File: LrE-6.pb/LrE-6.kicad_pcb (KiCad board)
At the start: 2 copper layers, 100 x 100 mm, 112 parts, among them J1 USB_B_Micro, J2 SM06B-SRSS-TB, Q1 2N7002, SW1 Tact_SW_8mm, SW10 Tact_SW_8mm, SW11 EC11_SMD, SW12 EC11_SMD, SW13 EC11_SMD, SW14 EC11_SMD, SW15 EC11_SMD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

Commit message: First commit for F3.2PB
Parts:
- C1, C10, C11, C12, C2, C3, C4, C5, C6, C7, C8, C9, R10, R11, R12, R13, R14, R15, R16, R5, R6, R7, R8, R9: moved to B.Cu
- SW11, SW12, SW13, SW14, SW15, SW16: footprint LrE-6:RotaryEncoder_EC11E-SMD2 -> Rotary_Encoder:RotaryEncoder_Alps_EC11E-Switch_Vertical_H20mm
- moved D16 0.86 mm to (105.2, 167.0)
- moved R13 0.11 mm to (184.7, 155.4)
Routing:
- net GND: track 126.7 -> 136.7 mm, vias 63 -> 65
- net +3V3: track 414.9 -> 407.7 mm
- net /ENC4-A: track 95.6 -> 92.1 mm
- net /ENC5-B: track 112.5 -> 109.2 mm
- net Net-(D11-Pad2): track 3.71 -> 6.80 mm
- net /ENC1-B: track 84.1 -> 87.1 mm, vias 1 -> 0
- net /L0: track 121.9 -> 119.1 mm
- net /LED1OUT: track 35.4 -> 38.1 mm
- net /L3: track 132.9 -> 130.3 mm, vias 7 -> 4
- net /ENC2-B: track 54.0 -> 56.2 mm
- net /ENC2-A: track 43.5 -> 45.8 mm
- net /L2: track 158.4 -> 156.3 mm, vias 3 -> 2
- net Net-(D15-Pad2): track 2.90 -> 5.02 mm
- net /VBUS: track 265.8 -> 267.8 mm
- net Net-(D16-Pad2): track 2.31 -> 4.23 mm
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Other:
- board text added: "F3.2"
- board text removed: "-1"
- board text removed: "F2.8"

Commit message: F3.2 add coper por inhibit
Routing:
- net GND: vias 65 -> 66

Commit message: F3.2 commit for order pb
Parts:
- gave numbers to parts that had none: 1
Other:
- board text added: "OLED"
- board text added: "for MIDI2LR"

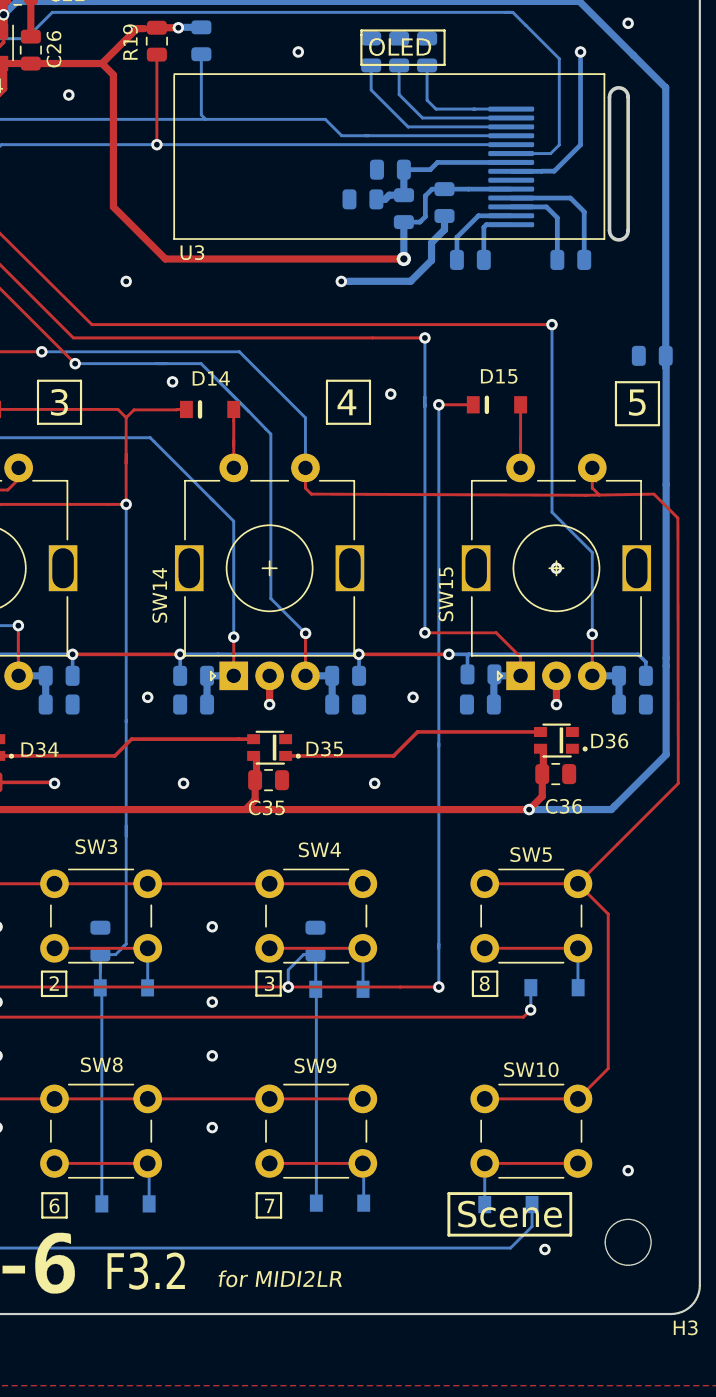
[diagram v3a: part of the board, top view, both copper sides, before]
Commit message: Rename LrE-6.pb F3.2 to F2.8-2
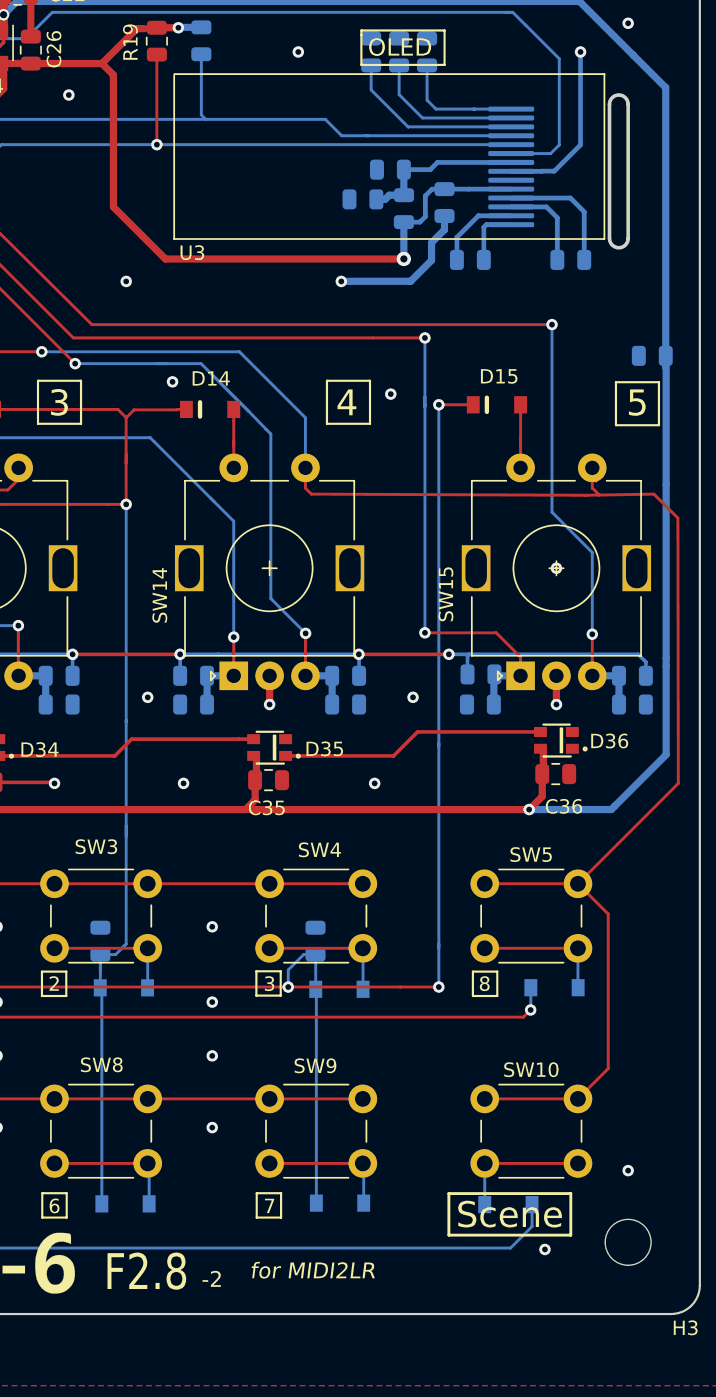
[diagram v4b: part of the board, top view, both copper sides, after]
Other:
- outline, holes or cut-outs redrawn
- board text added: "-2"
- board text added: "F2.8"
- board text removed: "F3.2"
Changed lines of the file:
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@@
-(kicad_pcb (version 20171130) (host pcbnew "(5.1.6)-1")
+(kicad_pcb (version 20171130) (host pcbnew "(5.1.6-0)")
   (general
     (thickness 1.2)
-    (drawings 120)
+    (drawings 121)
     (tracks 1270)
     (zones 0)
@@
     (add_net +3V3)
   )
+  (module LrE-6:OLED-9.1 locked (layer F.Cu)
+    (at 163.3462 113.5419)
+    (fp_text reference U3 (at 1.2638 12.4881) (layer F.SilkS)
+      (effects (font (size 1 1) (thickness 0.15)))
+    )
+    (fp_text value SSD1306_OLED_0.91 (at 8.9 -1.1) (layer F.Fab)
+      (effects (font (size 1 1) (thickness 0.15)))
+    )
+    (fp_circle (center 21 10.5) (end 21.2 10.5) (layer B.SilkS) (width 0.25))
+    (fp_line (start 30 0) (end 0 0) (layer F.SilkS) (width 0.12))
+    (fp_line (start 30 11.5) (end 30 0) (layer F.SilkS) (width 0.12))
+    (fp_line (start 0 11.5) (end 30 11.5) (layer F.SilkS) (width 0.12))
+    (fp_line (start 0 0.1) (end 0 11.5) (layer F.SilkS) (width 0.12))
+    (pad 11 smd roundrect (at 23.5 4.3) (size 3.2 0.35) (layers B.Cu B.Paste B.Mask) (roundrect_rratio 0.25)
+      (net 25 /SDA))
+    (pad 1 smd roundrect (at 23.5 10.5) (size 3.2 0.35) (layers B.Cu B.Paste B.Mask) (roundrect_rratio 0.25)
+      (net 39 "Net-(C23-Pad2)"))
+    (pad 2 smd roundrect (at 23.5 9.88) (size 3.2 0.35) (layers B.Cu B.Paste B.Mask) (roundrect_rratio 0.25)
+      (net 40 "Net-(C23-Pad1)"))
+    (pad 3 smd roundrect (at 23.5 9.26) (size 3.2 0.35) (layers B.Cu B.Paste B.Mask) (roundrect_rratio 0.25)
+      (net 38 "Net-(C24-Pad2)"))
+    (pad 4 smd roundrect (at 23.5 8.64) (size 3.2 0.35) (layers B.Cu B.Paste B.Mask) (roundrect_rratio 0.25)
+      (net 59 "Net-(C24-Pad1)"))
+    (pad 5 smd roundrect (at 23.5 8.02) (size 3.2 0.35) (layers B.Cu B.Paste B.Mask) (roundrect_rratio 0.25)
+      (net 22 +3V3))
+    (pad 6 smd roundrect (at 23.5 7.4) (size 3.2 0.35) (layers B.Cu B.Paste B.Mask) (roundrect_rratio 0.25)
+      (net 76 "Net-(U3-Pad6)"))
+    (pad 7 smd roundrect (at 23.5 6.78) (size 3.2 0.35) (layers B.Cu B.Paste B.Mask) (roundrect_rratio 0.25)
+      (net 4 GND))
+    (pad 8 smd roundrect (at 23.5 6.16) (size 3.2 0.35) (layers B.Cu B.Paste B.Mask) (roundrect_rratio 0.25)
+      (net 77 "Net-(C27-Pad2)"))
+    (pad 9 smd roundrect (at 23.5 5.54) (size 3.2 0.35) (layers B.Cu B.Paste B.Mask) (roundrect_rratio 0.25)
+      (net 27 /NRST))
+    (pad 10 smd roundrect (at 23.5 4.92) (size 3.2 0.35) (layers B.Cu B.Paste B.Mask) (roundrect_rratio 0.25)
+      (net 26 /SCL))
+    (pad 12 smd roundrect (at 23.5 3.68) (size 3.2 0.35) (layers B.Cu B.Paste B.Mask) (roundrect_rratio 0.25)
+      (net 60 "Net-(R18-Pad1)"))
+    (pad 13 smd roundrect (at 23.5 3.06) (size 3.2 0.35) (layers B.Cu B.Paste B.Mask) (roundrect_rratio 0.25)
+      (net 61 "Net-(C29-Pad2)"))
+    (pad 14 smd roundrect (at 23.5 2.44) (size 3.2 0.35) (layers B.Cu B.Paste B.Mask) (roundrect_rratio 0.25)
+      (net 62 "Net-(C28-Pad2)"))
+    (pad "" np_thru_hole oval (at 31 6.75) (size 1.6 10.8) (drill oval 1.2 10.4) (layers *.Cu *.Mask))
+  )
   (module Rotary_Encoder:RotaryEncoder_Alps_EC11E-Switch_Vertical_H20mm locked (layer F.Cu)
     (at 187.5 155.5 90)
@@
       (net 30 /VBUS))
   )
-  (module LrE-6:OLED-9.1 locked (layer F.Cu)
-    (at 163.3462 113.5419)
-    (fp_text reference U3 (at 1.2638 12.4881) (layer F.SilkS)
-      (effects (font (size 1 1) (thickness 0.15)))
-    )
-    (fp_text value SSD1306_OLED_0.91 (at 8.9 -1.1) (layer F.Fab)
-      (effects (font (size 1 1) (thickness 0.15)))
-    )
-    (fp_circle (center 21 10.5) (end 21.2 10.5) (layer B.SilkS) (width 0.25))
-    (fp_line (start 30 0) (end 0 0) (layer F.SilkS) (width 0.12))
-    (fp_line (start 30 11.5) (end 30 0) (layer F.SilkS) (width 0.12))
-    (fp_line (start 0 11.5) (end 30 11.5) (layer F.SilkS) (width 0.12))
-    (fp_line (start 0 0.1) (end 0 11.5) (layer F.SilkS) (width 0.12))
-    (pad 11 smd roundrect (at 23.5 4.3) (size 3.2 0.35) (layers B.Cu B.Paste B.Mask) (roundrect_rratio 0.25)
-      (net 25 /SDA))
-    (pad 1 smd roundrect (at 23.5 10.5) (size 3.2 0.35) (layers B.Cu B.Paste B.Mask) (roundrect_rratio 0.25)
-      (net 39 "Net-(C23-Pad2)"))
-    (pad 2 smd roundrect (at 23.5 9.88) (size 3.2 0.35) (layers B.Cu B.Paste B.Mask) (roundrect_rratio 0.25)
-      (net 40 "Net-(C23-Pad1)"))
-    (pad 3 smd roundrect (at 23.5 9.26) (size 3.2 0.35) (layers B.Cu B.Paste B.Mask) (roundrect_rratio 0.25)
-      (net 38 "Net-(C24-Pad2)"))
-    (pad 4 smd roundrect (at 23.5 8.64) (size 3.2 0.35) (layers B.Cu B.Paste B.Mask) (roundrect_rratio 0.25)
-      (net 59 "Net-(C24-Pad1)"))
-    (pad 5 smd roundrect (at 23.5 8.02) (size 3.2 0.35) (layers B.Cu B.Paste B.Mask) (roundrect_rratio 0.25)
-      (net 22 +3V3))
-    (pad 6 smd roundrect (at 23.5 7.4) (size 3.2 0.35) (layers B.Cu B.Paste B.Mask) (roundrect_rratio 0.25)
-      (net 76 "Net-(U3-Pad6)"))
-    (pad 7 smd roundrect (at 23.5 6.78) (size 3.2 0.35) (layers B.Cu B.Paste B.Mask) (roundrect_rratio 0.25)
-      (net 4 GND))
-    (pad 8 smd roundrect (at 23.5 6.16) (size 3.2 0.35) (layers B.Cu B.Paste B.Mask) (roundrect_rratio 0.25)
-      (net 77 "Net-(C27-Pad2)"))
-    (pad 9 smd roundrect (at 23.5 5.54) (size 3.2 0.35) (layers B.Cu B.Paste B.Mask) (roundrect_rratio 0.25)
-      (net 27 /NRST))
-    (pad 10 smd roundrect (at 23.5 4.92) (size 3.2 0.35) (layers B.Cu B.Paste B.Mask) (roundrect_rratio 0.25)
-      (net 26 /SCL))
-    (pad 12 smd roundrect (at 23.5 3.68) (size 3.2 0.35) (layers B.Cu B.Paste B.Mask) (roundrect_rratio 0.25)
-      (net 60 "Net-(R18-Pad1)"))
-    (pad 13 smd roundrect (at 23.5 3.06) (size 3.2 0.35) (layers B.Cu B.Paste B.Mask) (roundrect_rratio 0.25)
-      (net 61 "Net-(C29-Pad2)"))
-    (pad 14 smd roundrect (at 23.5 2.44) (size 3.2 0.35) (layers B.Cu B.Paste B.Mask) (roundrect_rratio 0.25)
-      (net 62 "Net-(C28-Pad2)"))
-    (pad "" np_thru_hole oval (at 31 6.25) (size 1.6 10.8) (drill oval 1.2 10.4) (layers *.Cu *.Mask))
-  )
   (module Resistor_SMD:R_0805_2012Metric (layer F.Cu)
     (at 162.14 111.2475 270)
@@
     )
   )
-  (gr_text "for MIDI2LR" (at 170.7 197.6) (layer F.SilkS)
+  (gr_text -2 (at 166 197.6) (layer F.SilkS)
+    (effects (font (size 1.1 1.1) (thickness 0.15)))
+  )
+  (gr_text "for MIDI2LR" (at 173 197) (layer F.SilkS)
     (effects (font (size 1.1 1.1) (thickness 0.15) italic))
   )
@@
     (effects (font (size 1.2 1.2) (thickness 0.3)))
   )
-  (gr_arc (start 194.35 124.45) (end 195 124.45) (angle 180) (layer Edge.Cuts) (width 0.25))
-  (gr_arc (start 194.35 115.15) (end 193.7 115.15) (angle 180) (layer Edge.Cuts) (width 0.25))
-  (gr_line (start 195 115.15) (end 195 124.45) (layer Edge.Cuts) (width 0.25))
-  (gr_line (start 193.7 124.45) (end 193.7 115.15) (layer Edge.Cuts) (width 0.25))
+  (gr_arc (start 194.35 125) (end 195 125) (angle 180) (layer Edge.Cuts) (width 0.25))
+  (gr_arc (start 194.35 115.65) (end 193.7 115.65) (angle 180) (layer Edge.Cuts) (width 0.25))
+  (gr_line (start 195 115.65) (end 195 125) (layer Edge.Cuts) (width 0.25))
+  (gr_line (start 193.7 125) (end 193.7 115.65) (layer Edge.Cuts) (width 0.25))
   (gr_line (start 168.4024 102) (end 164.2114 102) (layer F.SilkS) (width 0.15))
   (gr_line (start 168.4024 104.1844) (end 168.4024 102) (layer F.SilkS) (width 0.15))
@@
     (effects (font (size 1 1) (thickness 0.15)))
   )
-  (gr_text F3.2 (at 161.4 197.1) (layer F.SilkS)
+  (gr_text F2.8 (at 161.4 197.1) (layer F.SilkS)
     (effects (font (size 2.5 2) (thickness 0.3)))
   )
@@
     (polygon
       (pts
-        (xy 193.7 114.046) (xy 193.04 114.6) (xy 193.04 124.968) (xy 193.802 125.73) (xy 195 125.7)
-        (xy 195.58 124.9) (xy 195.6 114.7) (xy 194.9 114.046)
+        (xy 193.75 114.25) (xy 193 115) (xy 193.04 125.25) (xy 193.75 126.25) (xy 195 126.25)
+        (xy 195.58 125.25) (xy 195.6 115) (xy 194.9 114.25)
       )
     )
@@
     (polygon
       (pts
-        (xy 194.5 113.538) (xy 195.58 114.7) (xy 195.58 124.9) (xy 195 125.7046) (xy 193.7639 125.7046)
-        (xy 193.294 125.1712) (xy 163.2331 125.1458) (xy 163.2585 113.4364)
+        (xy 194.5 113.538) (xy 195.58 114.7) (xy 195.58 125.25) (xy 195 126.25) (xy 193.75 126.25)
+        (xy 193 125.25) (xy 163.2331 125.1458) (xy 163.2585 113.4364)
       )
     )
